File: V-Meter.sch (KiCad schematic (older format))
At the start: 6 parts

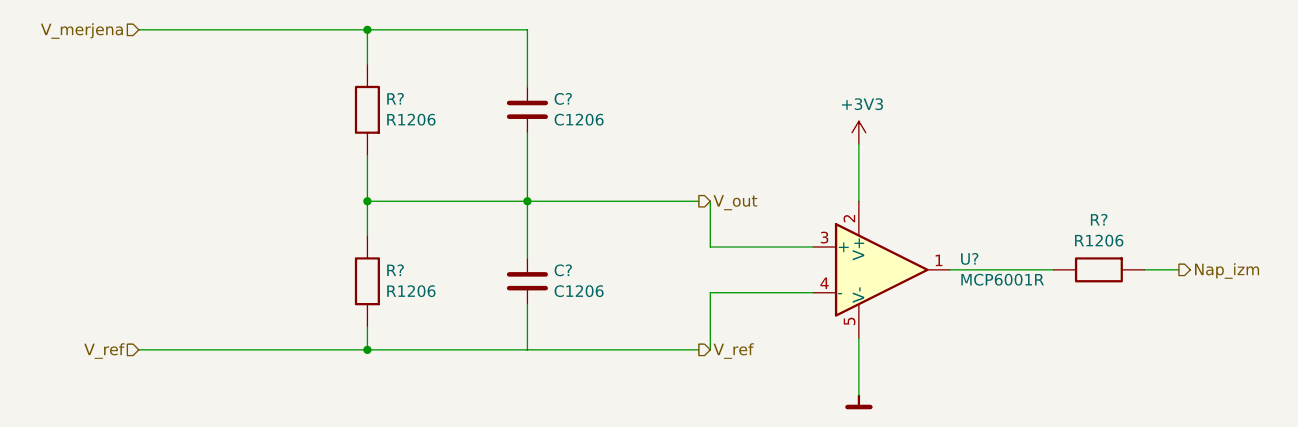
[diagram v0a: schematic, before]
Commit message: Dokončal V-meter sheet in dodal A-meter sheet
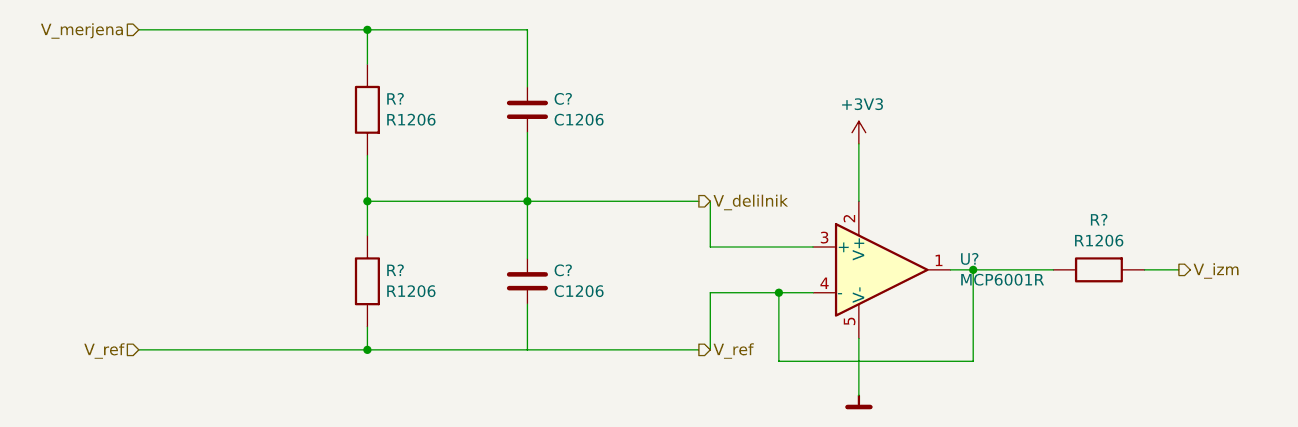
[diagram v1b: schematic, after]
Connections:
- net labels added: V_delilnik, V_izm
- net labels removed: Nap_izm, V_out
- wire segments 23 -> 28
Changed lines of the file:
@@
 $Descr A4 11693 8268
 encoding utf-8
-Sheet 4 4
+Sheet 4 5
 Title ""
 Date ""
@@
 	3500 2150 3500 2400
 Text HLabel 4250 2150 2    50   Output ~ 0
-V_out
+V_delilnik
 Wire Wire Line
 	3500 2150 4250 2150
@@
 	4300 2800 4300 2550
 Wire Wire Line
-	4300 2550 4750 2550
+	4300 2550 4600 2550
 Wire Wire Line
 	4300 2150 4300 2350
@@
 $EndComp
 Wire Wire Line
-	5350 2450 5800 2450
+	5350 2450 5450 2450
 Text HLabel 6350 2450 2    50   Output ~ 0
-Nap_izm
+V_izm
 Wire Wire Line
 	6200 2450 6350 2450
@@
 Wire Wire Line
 	4950 1900 4950 2150
+Wire Wire Line
+	4600 2550 4600 2850
+Wire Wire Line
+	4600 2850 5450 2850
+Wire Wire Line
+	5450 2850 5450 2450
+Connection ~ 4600 2550
+Wire Wire Line
+	4600 2550 4750 2550
+Connection ~ 5450 2450
+Wire Wire Line
+	5450 2450 5800 2450
 $EndSCHEMATC
